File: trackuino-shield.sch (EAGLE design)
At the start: 26 parts, among them IC2 REG1117, IC3 ON M74VHC1GT125DT1G, IC4 ON M74VHC1GT125DT1G, IC5 ON M74VHC1GT125DT1G, J5 J5MM, J6 J5MM, J7 J5MM, J8 J5MM, M2 HX1, Q1 PMV20XN, PMV16UN, etc, U1 LM60 int, X1 BU-SMA-V, X2 Vin, X3 LM60 ext, X4 Buzzer

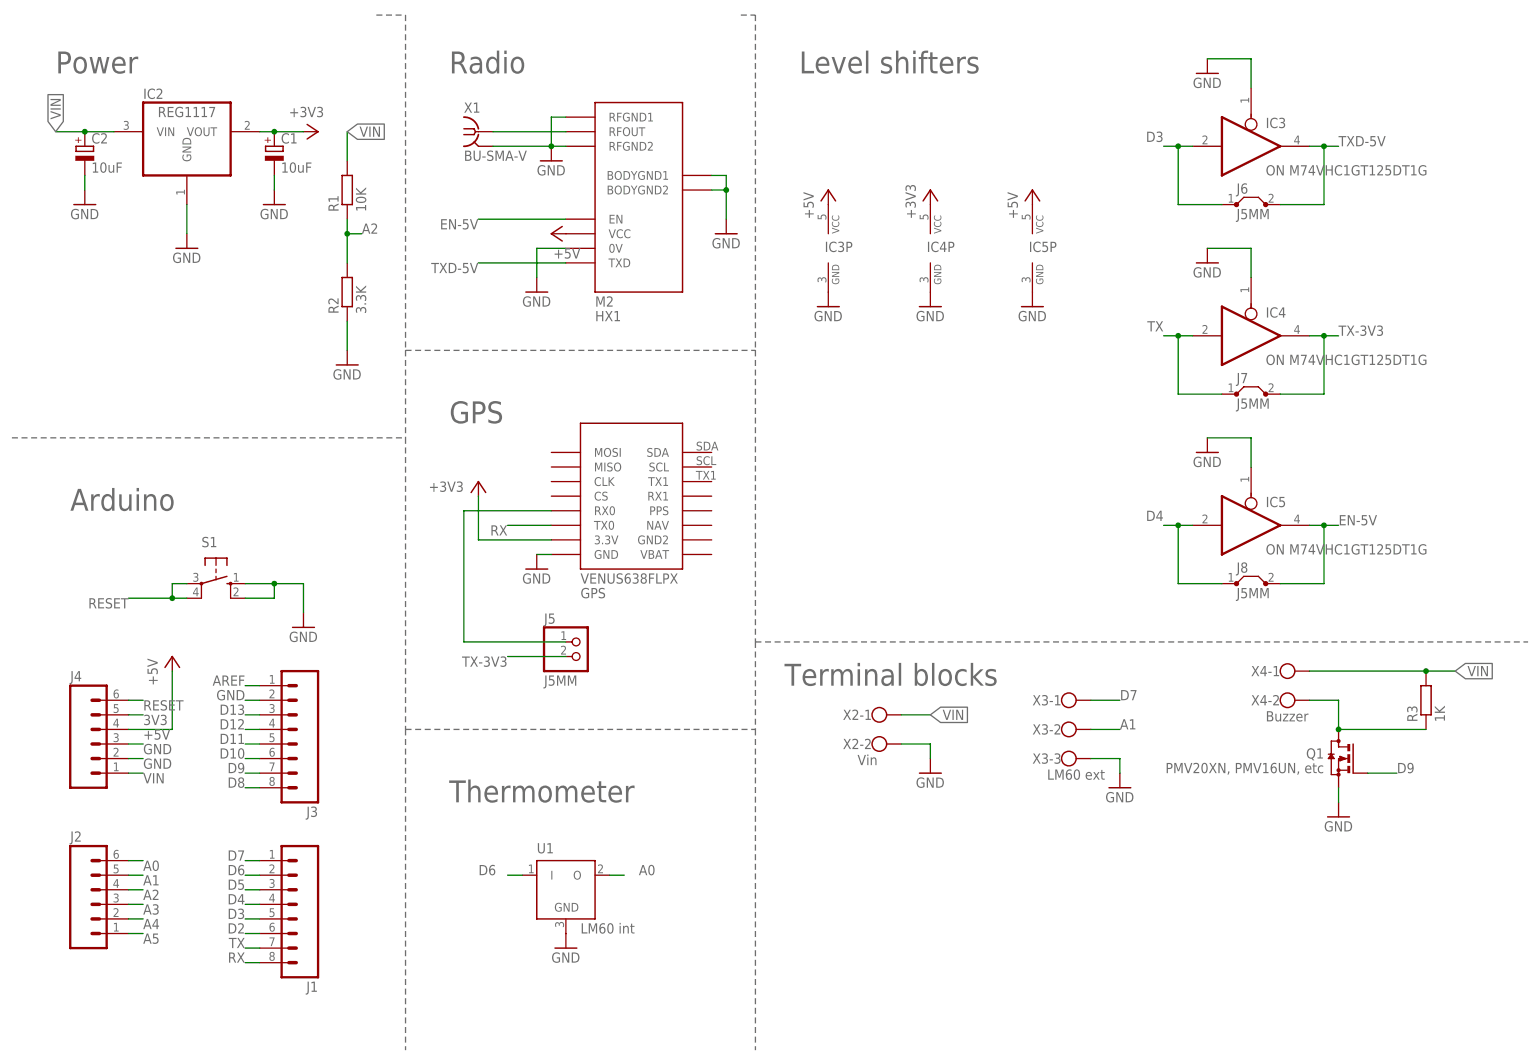
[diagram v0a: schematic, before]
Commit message: removing the level shifters
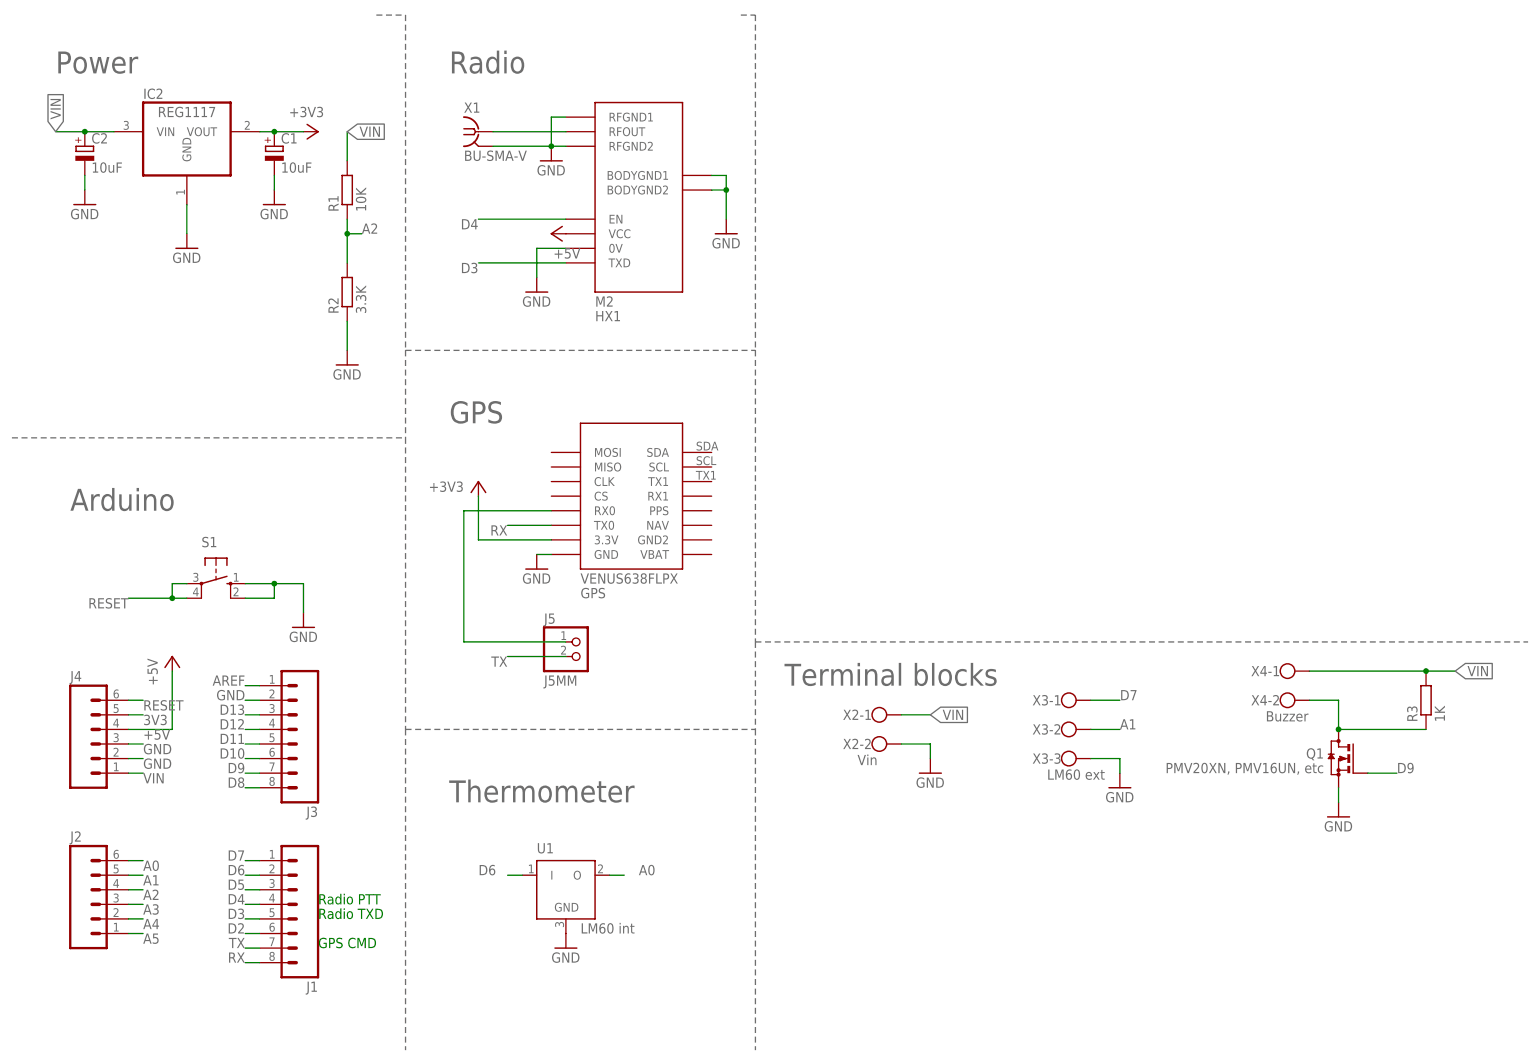
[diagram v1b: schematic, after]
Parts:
- removed IC3, IC4, IC5: ON M74VHC1GT125DT1G, 74xx-little-us:74AHC1G125DBV
- removed J6, J7, J8: J5MM, jumper:J5MM
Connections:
- removed net EN-5V: IC5A.O, J8.2, M2.EN
- removed net TX-3V3: IC4A.O, J5.2, J7.2
- removed net TXD-5V: IC3A.O, J6.2, M2.TXD
- net +3V3: no longer IC4P.VCC
- net +5V: no longer IC3P.VCC, IC5P.VCC
- net D3: now also M2.TXD; no longer IC3A.I, J6.1
- net D4: now also M2.EN; no longer IC5A.I, J8.1
- net GND: no longer IC3A.OE, IC3P.GND, IC4A.OE, IC4P.GND, IC5A.OE, IC5P.GND
- net TX: now also J5.2; no longer IC4A.I, J7.1
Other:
- note added: "GPS CMD"
- note added: "Radio PTT"
- note added: "Radio TXD"
- note removed: "Level shifters"

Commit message: Successfully replaced all surface mount components.
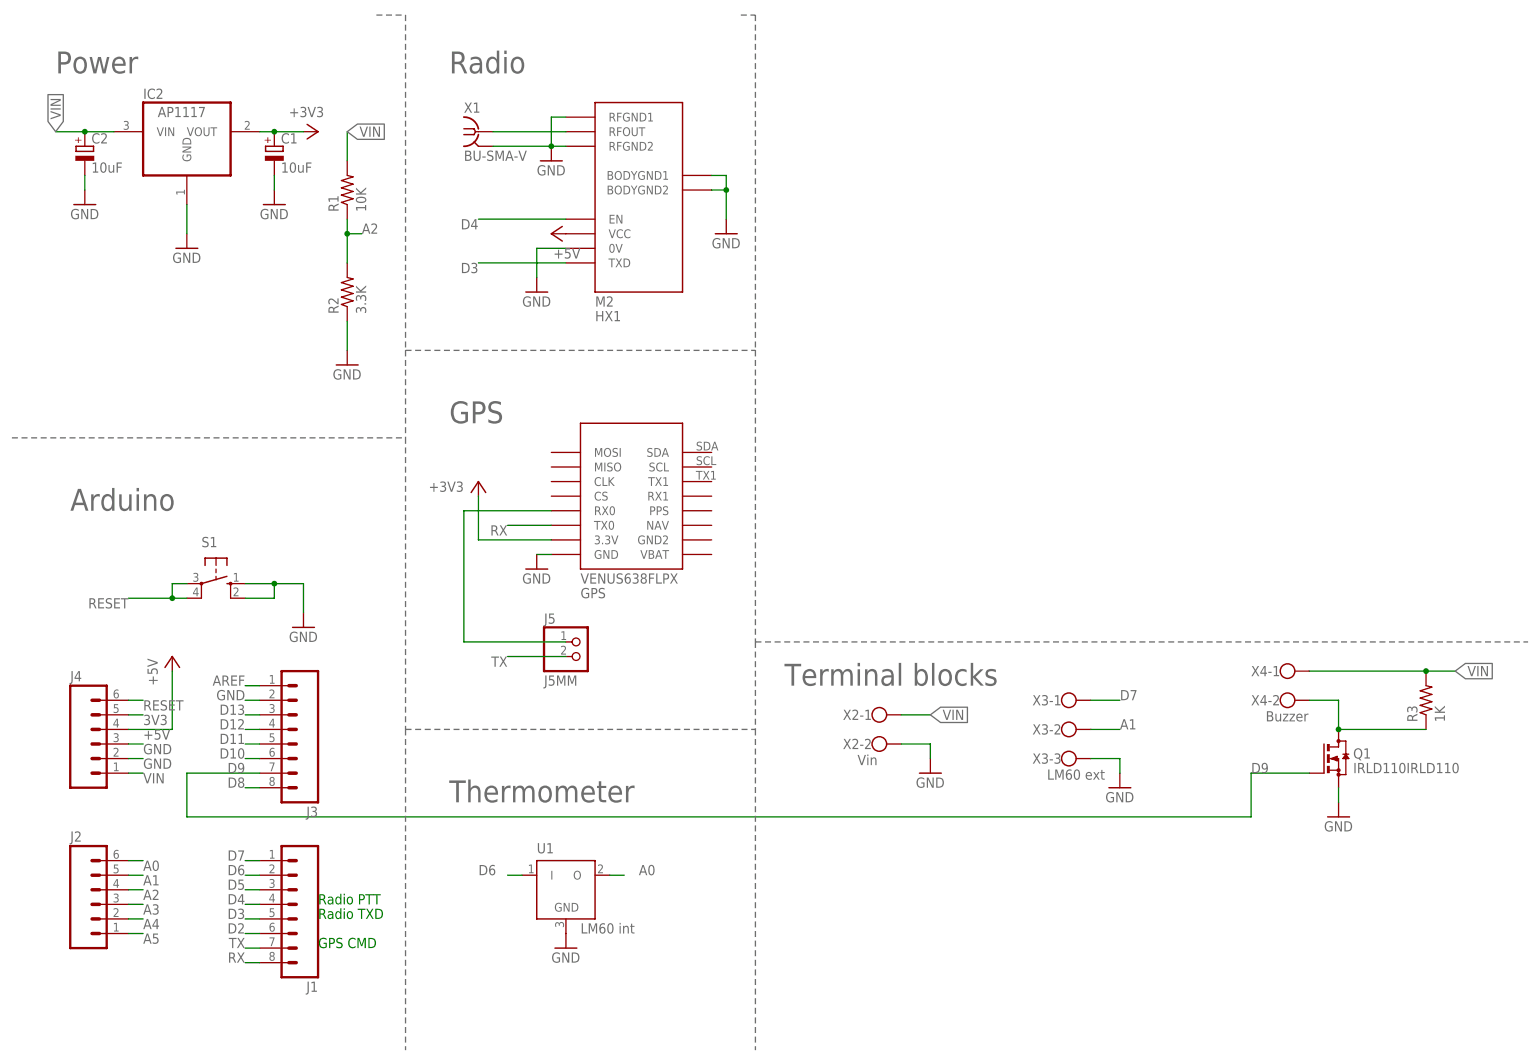
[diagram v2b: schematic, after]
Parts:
- IC2: value REG1117 -> AP1117; device burr-brown:REG1117 -> First:AP1117
- Q1: value PMV20XN, PMV16UN, etc -> IRLD110IRLD110; device transistor-small-signal:BSS123 -> First:IRLD110IRLD110
- R1, R2, R3: device resistor:R-EU_R1206 -> rcl:R-US_0207/7
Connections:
- net D9: no longer Q1.G
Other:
- moved on the sheet: Q1
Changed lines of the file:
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@@
 <part name="J5" library="pinhead" deviceset="PINHD-1X2" device="" value="J5MM"/>
 <part name="GND20" library="supply1" deviceset="GND" device=""/>
-<part name="R1" library="resistor" deviceset="R-EU_" device="R1206" value="10K"/>
-<part name="R2" library="resistor" deviceset="R-EU_" device="R1206" value="3.3K"/>
+<part name="R1" library="rcl" deviceset="R-US_" device="0207/7" value="10K"/>
+<part name="R2" library="rcl" deviceset="R-US_" device="0207/7" value="3.3K"/>
 <part name="GND21" library="supply1" deviceset="GND" device=""/>
-<part name="Q1" library="transistor-small-signal" deviceset="BSS123" device="" value="PMV20XN, PMV16UN, etc"/>
-<part name="R3" library="resistor" deviceset="R-EU_" device="R1206" value="1K"/>
-<part name="IC2" library="burr-brown" deviceset="REG1117" device=""/>
+<part name="R3" library="rcl" deviceset="R-US_" device="0207/7" value="1K"/>
+<part name="IC2" library="First" deviceset="AP1117" device=""/>
 <part name="GPS" library="trackuino" deviceset="VENUS638FLPX" device=""/>
+<part name="Q1" library="First" deviceset="IRLD110" device="IRLD110"/>
 </parts>
 <sheets>
@@
 <instance part="R2" gate="G$1" x="58.42" y="132.08" rot="R90"/>
 <instance part="GND21" gate="1" x="58.42" y="119.38"/>
-<instance part="Q1" gate="G$1" x="231.14" y="50.8" rot="MR0"/>
 <instance part="R3" gate="G$1" x="246.38" y="60.96" rot="R90"/>
-<instance part="IC2" gate="G$1" x="30.48" y="160.02"/>
+<instance part="IC2" gate="G$1" x="30.48" y="154.94"/>
 <instance part="GPS" gate="G$1" x="106.68" y="93.98"/>
+<instance part="Q1" gate="G$1" x="231.14" y="50.8"/>
 </instances>
 <busses>
@@
 <segment>
 <wire x1="231.14" y1="43.18" x2="231.14" y2="45.72" width="0.1524" layer="91"/>
+<pinref part="GND14" gate="1" pin="GND"/>
 <pinref part="Q1" gate="G$1" pin="S"/>
-<pinref part="GND14" gate="1" pin="GND"/>
 </segment>
 <segment>
@@
 <net name="D9" class="0">
 <segment>
-<wire x1="43.18" y1="48.26" x2="40.64" y2="48.26" width="0.1524" layer="91"/>
 <label x="40.64" y="48.26" size="1.778" layer="95" rot="MR0"/>
 <pinref part="J3" gate="G$1" pin="7"/>
-</segment>
-<segment>
-<wire x1="236.22" y1="48.26" x2="241.3" y2="48.26" width="0.1524" layer="91"/>
-<label x="241.3" y="48.26" size="1.778" layer="95"/>
-<pinref part="Q1" gate="G$1" pin="G"/>
+<wire x1="43.18" y1="48.26" x2="30.48" y2="48.26" width="0.1524" layer="91"/>
+<wire x1="30.48" y1="48.26" x2="30.48" y2="40.64" width="0.1524" layer="91"/>
+<wire x1="226.06" y1="48.26" x2="215.9" y2="48.26" width="0.1524" layer="91"/>
+<label x="215.9" y="48.26" size="1.778" layer="95"/>
+<wire x1="30.48" y1="40.64" x2="215.9" y2="40.64" width="0.1524" layer="91"/>
+<wire x1="215.9" y1="40.64" x2="215.9" y2="48.26" width="0.1524" layer="91"/>
 </segment>
 </net>
@@
 <wire x1="231.14" y1="60.96" x2="231.14" y2="55.88" width="0.1524" layer="91"/>
 <wire x1="231.14" y1="55.88" x2="246.38" y2="55.88" width="0.1524" layer="91"/>
+<pinref part="X4" gate="-2" pin="KL"/>
+<pinref part="R3" gate="G$1" pin="1"/>
+<pinref part="Q1" gate="G$1" pin="D"/>
 <junction x="231.14" y="55.88"/>
-<pinref part="X4" gate="-2" pin="KL"/>
-<pinref part="Q1" gate="G$1" pin="D"/>
-<pinref part="R3" gate="G$1" pin="1"/>
-</segment>
-</net>
+</segment>
+</net>

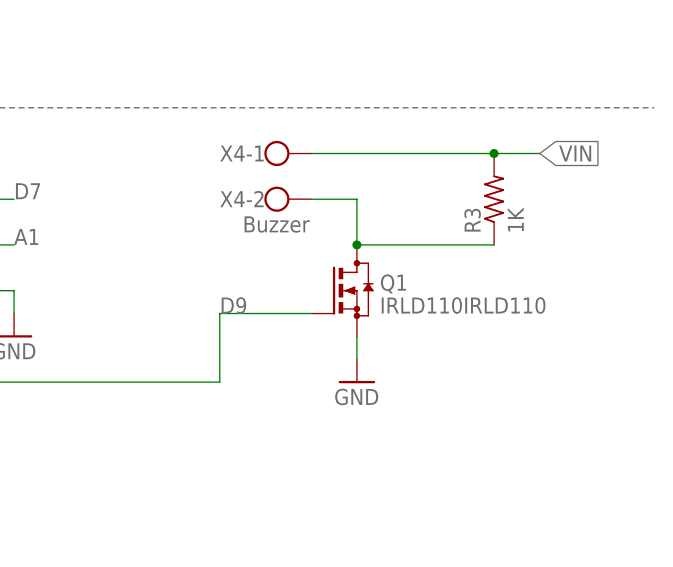
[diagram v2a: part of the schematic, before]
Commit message: Placed buzzer mosfet. All surface mount components have been removed
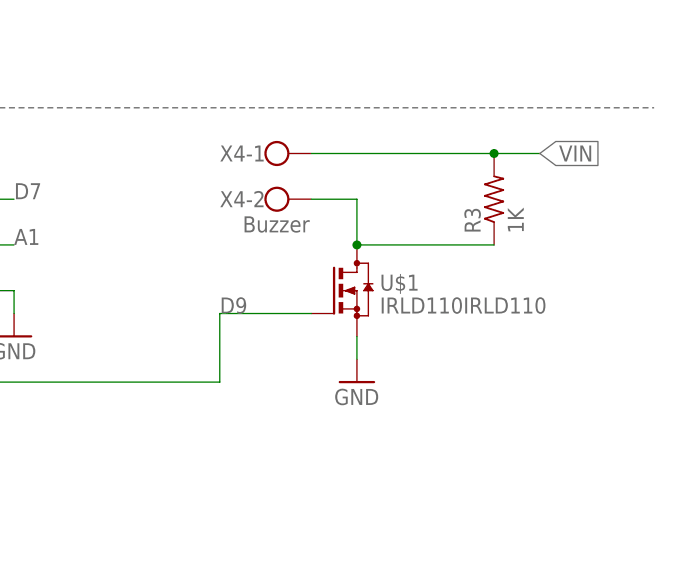
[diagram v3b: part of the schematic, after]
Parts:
- renumbered Q1 to U$1
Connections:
- net D9: now also U$1.G
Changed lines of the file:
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@@
 <?xml version="1.0" encoding="utf-8"?>
 <!DOCTYPE eagle SYSTEM "eagle.dtd">
-<eagle version="6.4">
+<eagle version="6.5.0">
 <drawing>
 <settings>
@@
 <part name="IC2" library="First" deviceset="AP1117" device=""/>
 <part name="GPS" library="trackuino" deviceset="VENUS638FLPX" device=""/>
-<part name="Q1" library="First" deviceset="IRLD110" device="IRLD110"/>
+<part name="U$1" library="First" deviceset="IRLD110" device="IRLD110"/>
 </parts>
 <sheets>
@@
 <instance part="IC2" gate="G$1" x="30.48" y="154.94"/>
 <instance part="GPS" gate="G$1" x="106.68" y="93.98"/>
-<instance part="Q1" gate="G$1" x="231.14" y="50.8"/>
+<instance part="U$1" gate="G$1" x="231.14" y="50.8"/>
 </instances>
 <busses>
@@
 <wire x1="231.14" y1="43.18" x2="231.14" y2="45.72" width="0.1524" layer="91"/>
 <pinref part="GND14" gate="1" pin="GND"/>
-<pinref part="Q1" gate="G$1" pin="S"/>
+<pinref part="U$1" gate="G$1" pin="S"/>
 </segment>
 <segment>
@@
 <wire x1="30.48" y1="40.64" x2="215.9" y2="40.64" width="0.1524" layer="91"/>
 <wire x1="215.9" y1="40.64" x2="215.9" y2="48.26" width="0.1524" layer="91"/>
+<pinref part="U$1" gate="G$1" pin="G"/>
 </segment>
 </net>
@@
 <pinref part="X4" gate="-2" pin="KL"/>
 <pinref part="R3" gate="G$1" pin="1"/>
-<pinref part="Q1" gate="G$1" pin="D"/>
+<pinref part="U$1" gate="G$1" pin="D"/>
 <junction x="231.14" y="55.88"/>
 </segment>

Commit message: Minor routing change
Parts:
- renumbered U$1 to Q1
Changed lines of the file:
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@@
 <part name="IC2" library="First" deviceset="AP1117" device=""/>
 <part name="GPS" library="trackuino" deviceset="VENUS638FLPX" device=""/>
-<part name="U$1" library="First" deviceset="IRLD110" device="IRLD110"/>
+<part name="Q1" library="First" deviceset="IRLD110" device="IRLD110"/>
 </parts>
 <sheets>
@@
 <instance part="IC2" gate="G$1" x="30.48" y="154.94"/>
 <instance part="GPS" gate="G$1" x="106.68" y="93.98"/>
-<instance part="U$1" gate="G$1" x="231.14" y="50.8"/>
+<instance part="Q1" gate="G$1" x="231.14" y="50.8"/>
 </instances>
 <busses>
@@
 <wire x1="231.14" y1="43.18" x2="231.14" y2="45.72" width="0.1524" layer="91"/>
 <pinref part="GND14" gate="1" pin="GND"/>
-<pinref part="U$1" gate="G$1" pin="S"/>
+<pinref part="Q1" gate="G$1" pin="S"/>
 </segment>
 <segment>
@@
 <wire x1="30.48" y1="40.64" x2="215.9" y2="40.64" width="0.1524" layer="91"/>
 <wire x1="215.9" y1="40.64" x2="215.9" y2="48.26" width="0.1524" layer="91"/>
-<pinref part="U$1" gate="G$1" pin="G"/>
+<pinref part="Q1" gate="G$1" pin="G"/>
 </segment>
 </net>
@@
 <pinref part="X4" gate="-2" pin="KL"/>
 <pinref part="R3" gate="G$1" pin="1"/>
-<pinref part="U$1" gate="G$1" pin="D"/>
+<pinref part="Q1" gate="G$1" pin="D"/>
 <junction x="231.14" y="55.88"/>
 </segment>
